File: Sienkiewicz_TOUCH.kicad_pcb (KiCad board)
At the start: 6 copper layers, 38 x 38 mm, 9 parts, among them J1 Conn_ARM_SWD_TagConnect_TC203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, U1 ATtiny204-SS

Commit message: board updatea
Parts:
- added C1: 100nF, Capacitor_SMD:C_1210_3225Metric, F.Cu at (161.5, 83.0)
- added Cd2: 100nF, Capacitor_SMD:C_1210_3225Metric, F.Cu at (133.5, 86.0)
- added Cs1: 2n2, Capacitor_SMD:C_0805_2012Metric, F.Cu at (133.5, 93.0)
- added P1: USB_C_Plug_USB2.0, __USB4135-GF-A:GCT_USB4135-GF-A_REVA, F.Cu at (148.5, 74.0)
- added R3: 1M, Resistor_SMD:R_0805_2012Metric, F.Cu at (133.5, 98.0)
- added Rs1: 4k3, Resistor_SMD:R_0805_2012Metric, F.Cu at (133.5, 95.0)
- added U2: AT42QT1012-T, Package_TO_SOT_SMD:SOT-23-6, F.Cu at (133.5, 90.0)
- B1: renamed from U2; value ~ -> BOARD_OUTLINE
- D2: footprint Diode_SMD:D_1206_3216Metric -> LED_SMD:LED_1206_3216Metric
- moved D2 31.8 mm to (143.5, 106.0)
- moved Rd1 16.3 mm to (156.5, 76.0)
- moved Rd2 16.3 mm to (140.5, 76.0)
- moved D1 15.0 mm to (153.5, 106.0), turned to 90 degrees
- moved R2 9.36 mm to (141.0, 106.0)
- moved R1 9.34 mm to (156.0, 106.0), turned to 90 degrees
- moved U1 0.53 mm to (161.5, 90.0)
- moved J1 0.36 mm to (148.5, 106.0)
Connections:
- D1 pad 1: GND -> Net-(D1-K)
- D1 pad 2: Net-(D1-A) -> LED1
- D2 pad 1: GND -> Net-(D2-K)
- R1 pad 1: Net-(U1-PA2) -> Net-(D1-K)
- R1 pad 2: Net-(D1-A) -> GND
- R2 pad 1: Net-(U1-PA3) -> Net-(D2-K)
- R2 pad 2: Net-(D2-A) -> GND
- U1 pad 12: Net-(U1-PA2) -> Net-(D2-A)
- U1 pad 13: Net-(U1-PA3) -> unconnected-(U1-PA3-Pad13)
- U1 pad 3: SR_SDI -> unconnected-(U1-PA5-Pad3)
- U1 pad 4: SR_CLK -> unconnected-(U1-PA6-Pad4)
- U1 pad 5: SR_LATCH -> /Project Architecture/Section B - uC/TT
- U1 pad 6: unconnected-(U1-PB3-Pad6) -> SR_CLK
- U1 pad 7: unconnected-(U1-PB2-Pad7) -> SR_LATCH
- U1 pad 8: unconnected-(U1-PB1-Pad8) -> LED1
- U1 pad 9: unconnected-(U1-PB0-Pad9) -> SR_SDI
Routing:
- net VCC: track 0.00 -> 87.9 mm, vias 0 -> 6
- net /Project Architecture/Section B - uC/TT: track 0.00 -> 47.4 mm
- net SR_SDI: track 0.00 -> 45.3 mm
- net SR_CLK: track 0.00 -> 32.5 mm
- net Net-(D2-A): track 0.00 -> 31.8 mm
- net /Project Architecture/Section B - uC/UPDI: track 0.00 -> 26.4 mm
- net SR_LATCH: track 0.00 -> 19.9 mm
- net LED1: track 0.00 -> 16.8 mm
- net /Project Architecture/Section C - Touch sensor/TOUCH: track 0.00 -> 8.50 mm, vias 0 -> 1
- net Net-(U2-SNSK): track 0.00 -> 4.14 mm
- net Net-(U2-SNS): track 0.00 -> 2.13 mm
- net GND: vias 0 -> 143
- added copper zone on B.Cu, net /Project Architecture/Section C - Touch sensor/TOUCH
- added copper zone on B.Cu, net GND
- added copper zone on F.Cu, net GND
- added copper zone on B.Cu, net VCC
- added copper zone on F.Cu, net VCC
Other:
- copper layers 6 -> 2
- board text added: "GND"
- board text added: "UPDI"
- board text added: "VCC"

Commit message: pcb update
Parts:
- removed P1: USB_C_Plug_USB2.0, __USB4135-GF-A:GCT_USB4135-GF-A_REVA
- added J2: USB4135-GF-A_REVA, __USB4135-GF-A:GCT_USB4135-GF-A_REVA, F.Cu at (148.5, 74.0)
- D1: footprint Diode_SMD:D_1206_3216Metric -> LED_SMD:LED_1206_3216Metric
- moved Rd1 16.0 mm to (140.5, 76.5)
- moved Rd2 16.0 mm to (156.5, 76.5)
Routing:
- net Net-(J2-VCONN): track 0.00 -> 9.01 mm
- net Net-(J2-CC): track 0.00 -> 9.01 mm
- net VCC: track 87.9 -> 87.1 mm
- net /Project Architecture/Section B - uC/TT: track 47.4 -> 46.9 mm
- net GND: vias 143 -> 156

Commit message: pcb update
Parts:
- added TP1: GND, TestPoint:TestPoint_Pad_D1.5mm, F.Cu at (131.5, 82.0)
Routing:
- net /Project Architecture/Section C - Touch sensor/TOUCH: track 8.50 -> 5.09 mm
- net Net-(D1-K): track 0.00 -> 3.30 mm
- net Net-(D2-K): track 0.00 -> 2.70 mm
- net GND: vias 156 -> 166

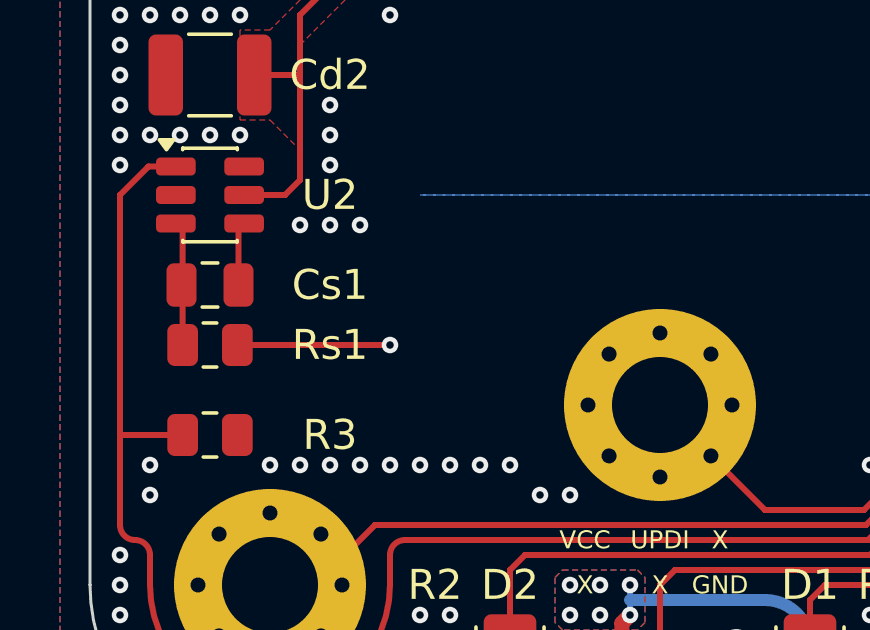
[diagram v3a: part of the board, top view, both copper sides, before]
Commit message: led1,led2 better documented
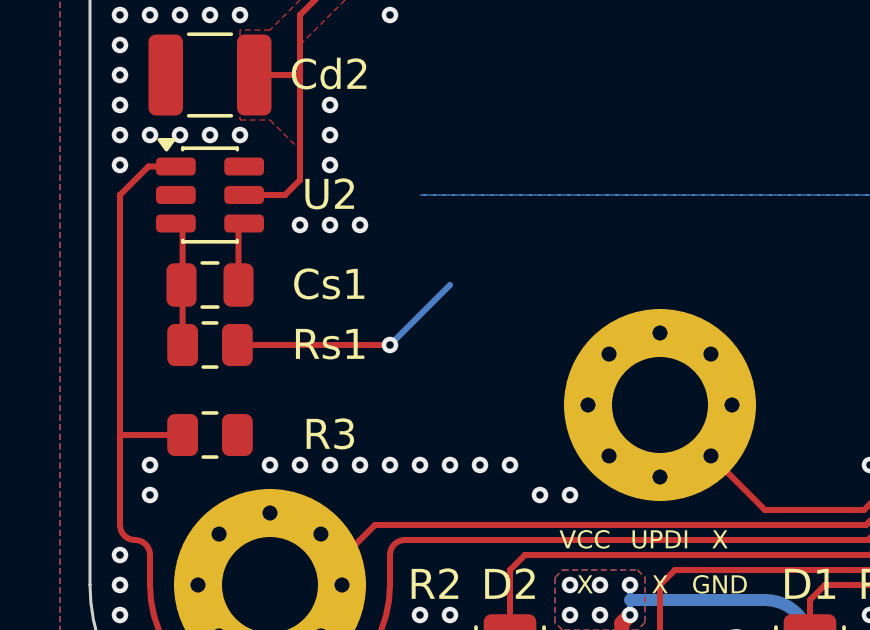
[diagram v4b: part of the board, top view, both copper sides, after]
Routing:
- net /Project Architecture/Section C - Touch sensor/TOUCH: track 5.09 -> 7.92 mm
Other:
- board text removed: "30°"
- board text removed: "3× 120°"

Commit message: touch pad library creation
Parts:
- added TouP1: TouchPad, __Touch_PAD:TouchPAD, B.Cu at (148.5, 90.0)
- moved TP1 1.00 mm to (131.5, 81.0)
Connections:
- net Net-(D2-A) renamed LED2
- net SR_CLK renamed /Project Architecture/Section B - uC/SR_CLK
- net SR_LATCH renamed /Project Architecture/Section B - uC/SR_LATCH
- net SR_SDI renamed /Project Architecture/Section B - uC/SR_SDI
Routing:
- net /Project Architecture/Section C - Touch sensor/TOUCH: track 7.92 -> 16.9 mm

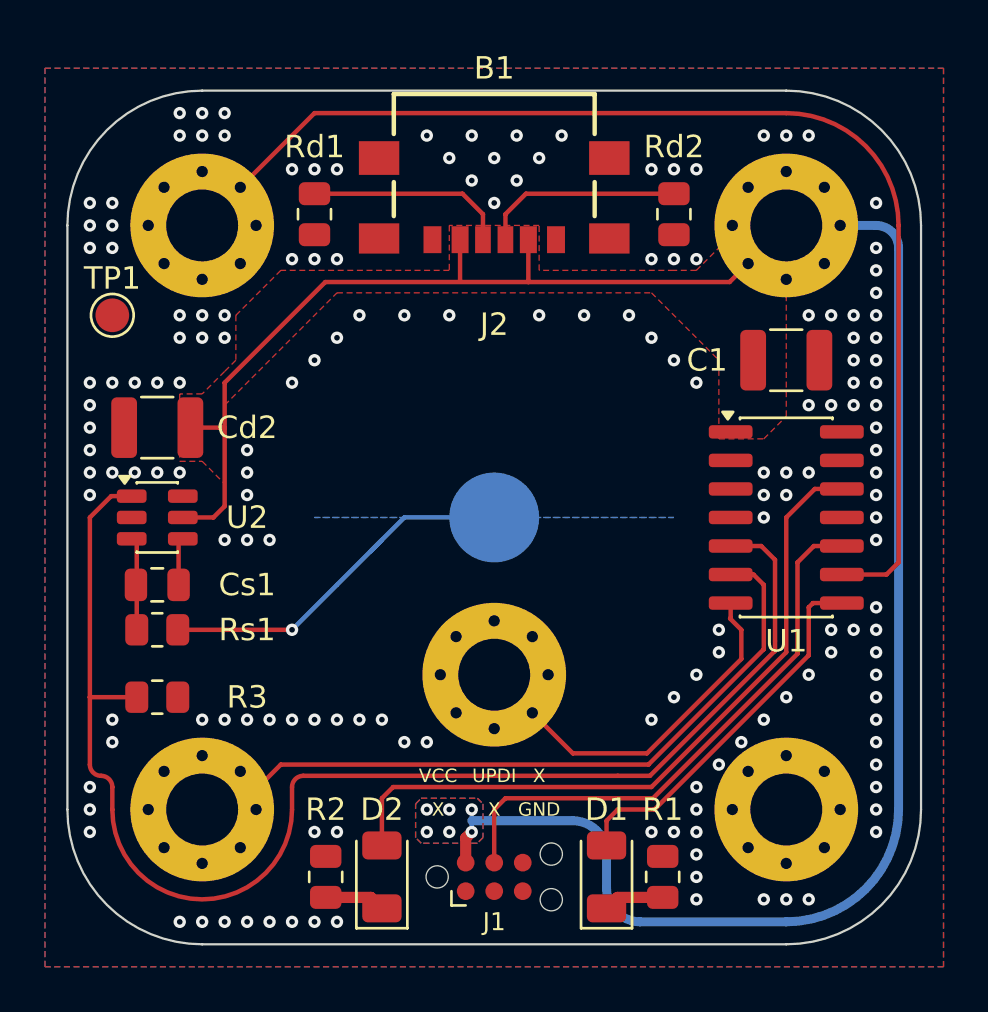
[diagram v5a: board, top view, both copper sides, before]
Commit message: minor updates of shematic and pcb and touch pad library
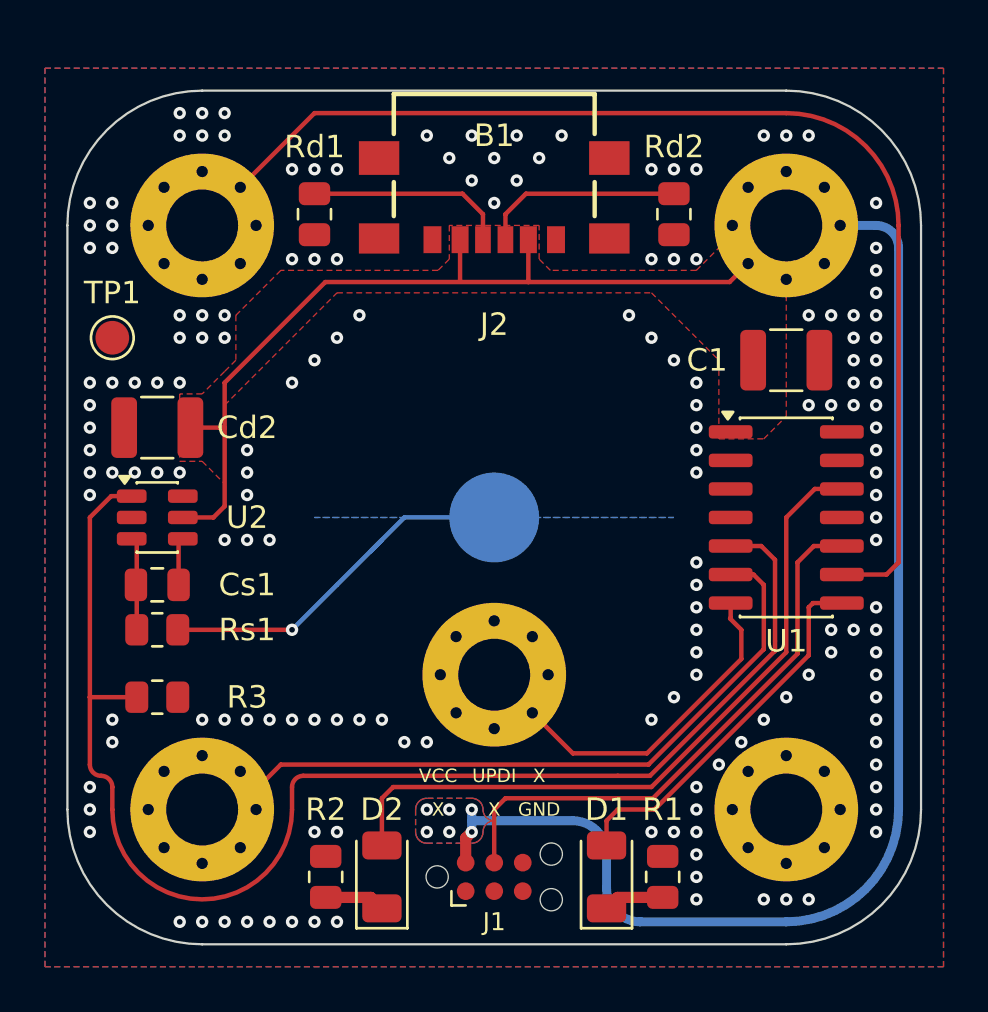
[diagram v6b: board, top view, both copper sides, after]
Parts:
- J1: value Conn_ARM_SWD_TagConnect_TC2030-NL -> TC2030-NL
- moved TP1 1.00 mm to (131.5, 82.0)
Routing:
- net GND: vias 166 -> 163

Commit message: [sch] update touch sensor section
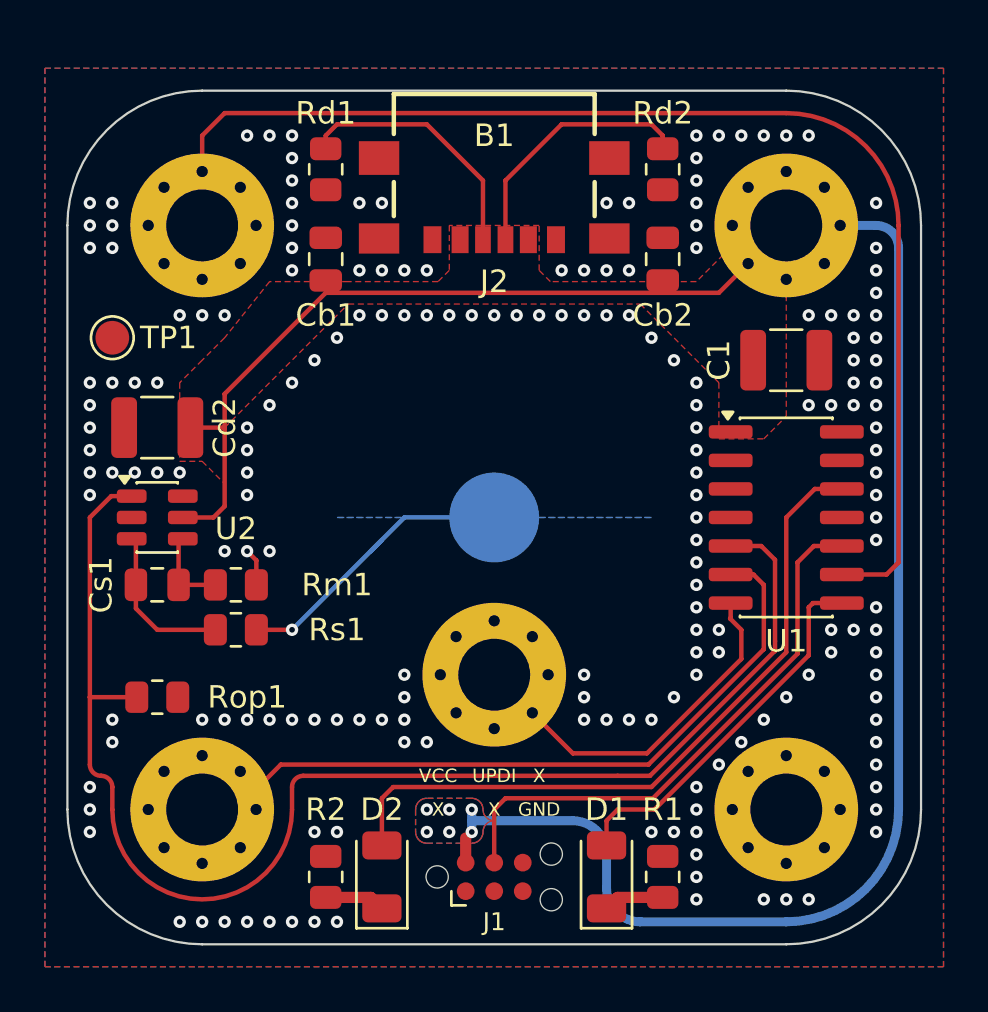
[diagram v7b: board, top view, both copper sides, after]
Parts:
- added Cb1: 1u/16V, Capacitor_SMD:C_0805_2012Metric, F.Cu at (141.0, 78.5)
- added Cb2: 1u/16V, Capacitor_SMD:C_0805_2012Metric, F.Cu at (156.0, 78.5)
- added Rm1: 1M, Resistor_SMD:R_0805_2012Metric, F.Cu at (137.0, 93.0)
- J1: value TC2030-NL -> Conn_ARM_SWD_TagConnect_TC2030-NL
- Rop1: renamed from R3; value 1M -> 100k
- moved Rs1 3.50 mm to (137.0, 95.0)
- moved Rd1 2.06 mm to (141.0, 74.5)
- moved Rd2 2.06 mm to (156.0, 74.5)
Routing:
- net VCC: track 87.1 -> 83.1 mm
- net Net-(U2-SNSK): track 4.14 -> 7.82 mm
- net /Project Architecture/Section C - Touch sensor/TOUCH: track 16.9 -> 13.4 mm
- net Net-(J2-VCONN): track 9.01 -> 11.5 mm
- net Net-(J2-CC): track 9.01 -> 11.5 mm
- net /Project Architecture/Section B - uC/SR_SDI: track 45.3 -> 47.6 mm
- net Net-(U2-SNS): track 2.13 -> 4.03 mm
- net GND: track 0.00 -> 1.67 mm, vias 163 -> 186
